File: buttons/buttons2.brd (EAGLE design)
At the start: 70 x 40 mm, 14 parts, among them U1 TINY2313

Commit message: I think I have a workable Cherry MX design
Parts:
- removed U1: TINY2313, avr-6:DIL20
- added U$1: TINY2313-*P*, avr-6:DIL20
- moved S6 166.9 mm to (55.0, 35.5)
- moved S5 143.9 mm to (39.0, 35.5)
- moved S3 124.5 mm to (55.0, 19.5)
- moved S4 121.0 mm to (23.0, 35.5)
- moved S2 102.7 mm to (39.0, 19.5)
- moved JP1 94.4 mm to (49.0, 7.91)
- moved S1 81.4 mm to (23.0, 19.5)
- moved C1 62.5 mm to (3.23, 8.81)
- moved SV1 23.0 mm to (26.1, 5.98), turned to 0 degrees
- moved STANDOFF3 4.44 mm to (66.2, 41.1)
- moved STANDOFF4 4.00 mm to (2.89, 41.1)
- moved STANDOFF1 1.12 mm to (66.2, 2.84)
- moved STANDOFF2 0.51 mm to (2.93, 2.84)
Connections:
- net BUTTON1: now also U$1.2; no longer U1.2
- net BUTTON2: now also U$1.3; no longer U1.3
- net BUTTON3: now also U$1.4; no longer U1.4
- net BUTTON4: now also U$1.5; no longer U1.5
- net BUTTON5: now also U$1.6; no longer U1.6
- net BUTTON6: now also U$1.7; no longer U1.7
- net GND: now also U$1.10; no longer U1.10
- net N$1: now also U$1.16; no longer U1.16
- net N$2: now also U$1.15; no longer U1.15
- net N$3: now also U$1.14; no longer U1.14
- net N$4: now also U$1.13; no longer U1.13
- net N$5: now also U$1.12; no longer U1.12
- net N$6: now also U$1.11; no longer U1.11
- net VCC: now also U$1.20; no longer U1.20
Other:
- board size 70 x 40 mm -> 69 x 44 mm

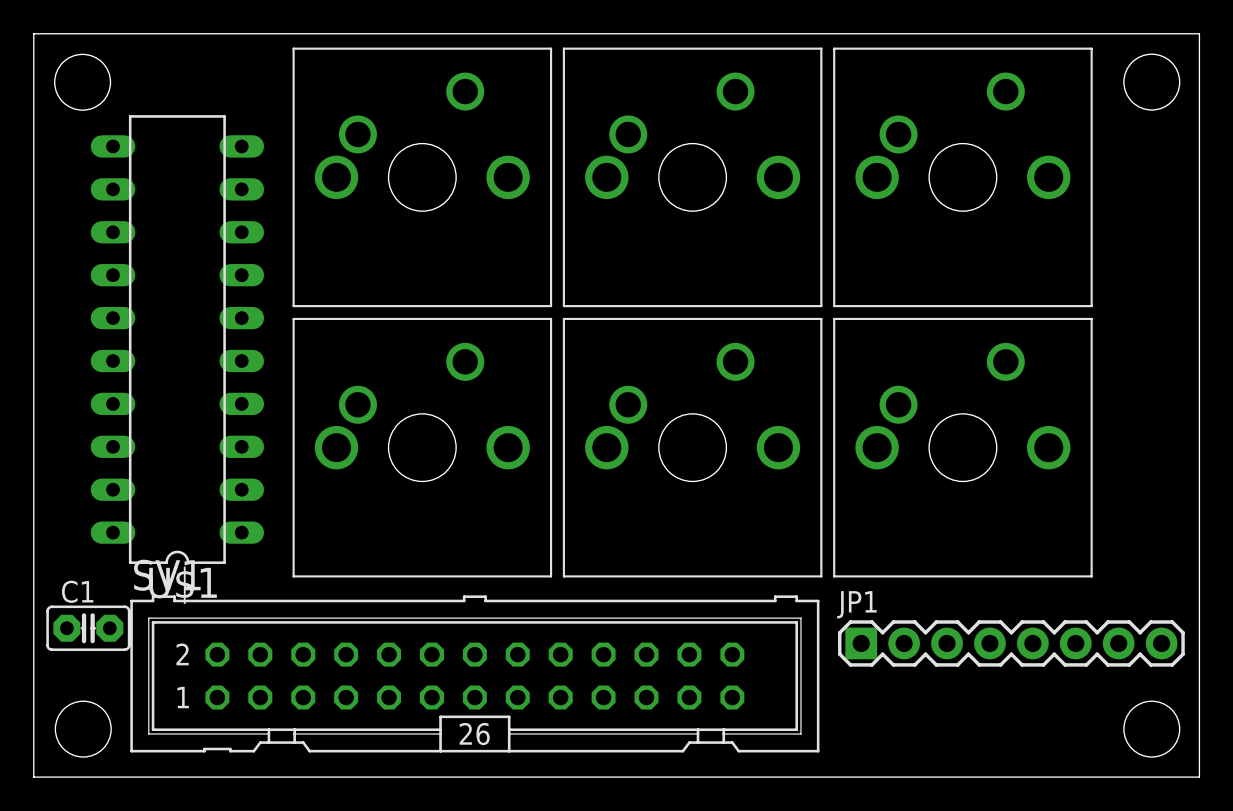
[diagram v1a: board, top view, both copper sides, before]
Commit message: working on signal routing
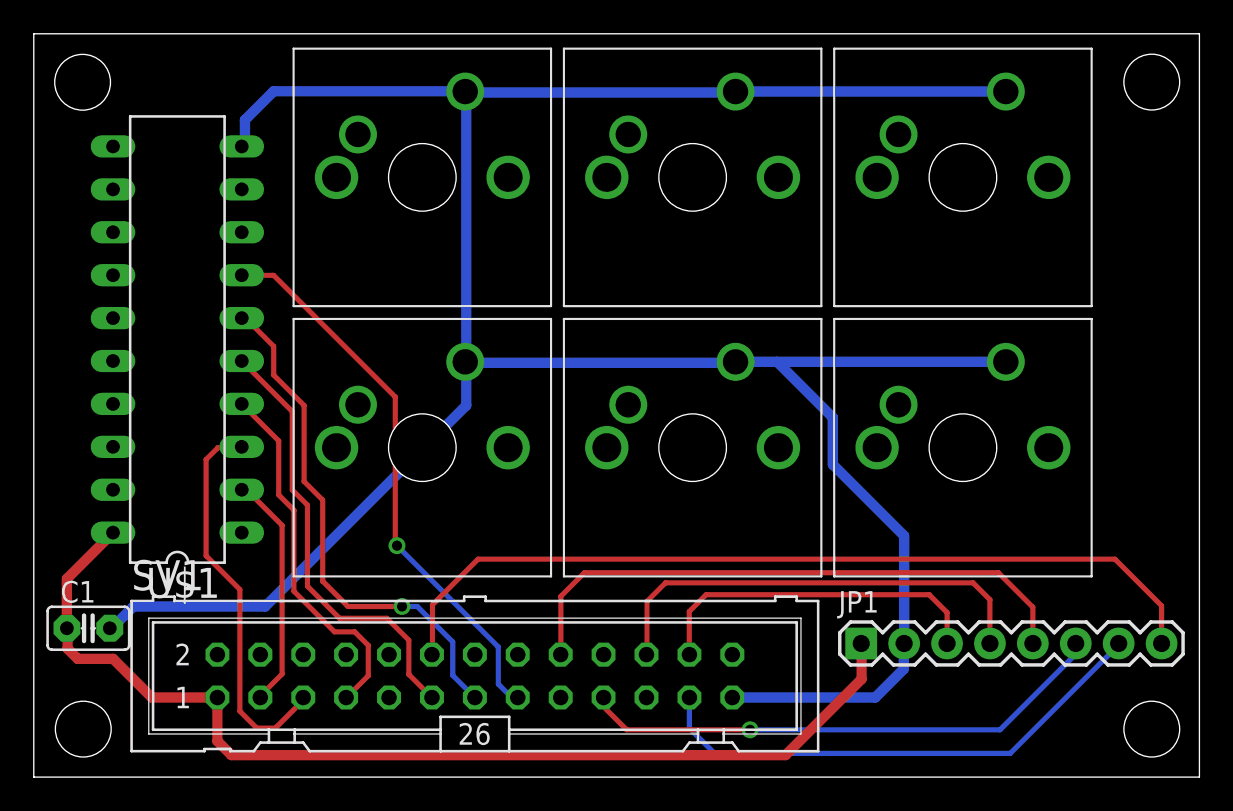
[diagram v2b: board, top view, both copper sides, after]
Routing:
- net GND: track 0.00 -> 156.8 mm
- net VCC: track 0.00 -> 63.1 mm
- net LED: track 0.00 -> 50.6 mm
- net DC: track 0.00 -> 35.0 mm
- net BUTTON6: track 0.00 -> 33.1 mm, vias 0 -> 1
- net MOSI: track 0.00 -> 31.6 mm, vias 0 -> 1
- net BUTTON5: track 0.00 -> 30.7 mm, vias 0 -> 1
- net SCK: track 0.00 -> 30.6 mm
- net RESET: track 0.00 -> 26.9 mm
- net BUTTON4: track 0.00 -> 26.2 mm
- net BUTTON2: track 0.00 -> 23.3 mm
- net BUTTON3: track 0.00 -> 21.7 mm
- net CS: track 0.00 -> 20.5 mm
- net BUTTON1: track 0.00 -> 14.0 mm

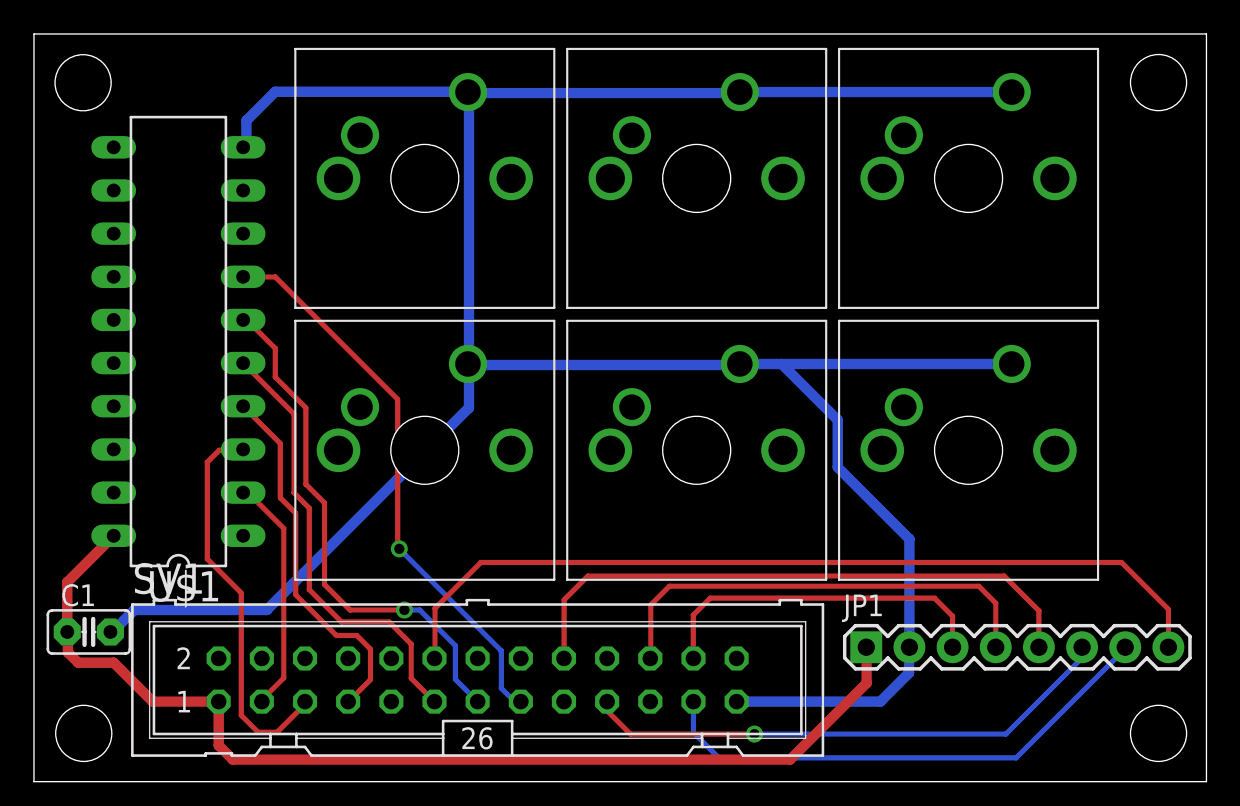
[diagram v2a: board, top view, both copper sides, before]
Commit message: rip up traces to buttons, move attiny2313
Buttons need to be mirrored because they will be
on the bottom of the board.

The attiny2313 was too close to the top left standoff.
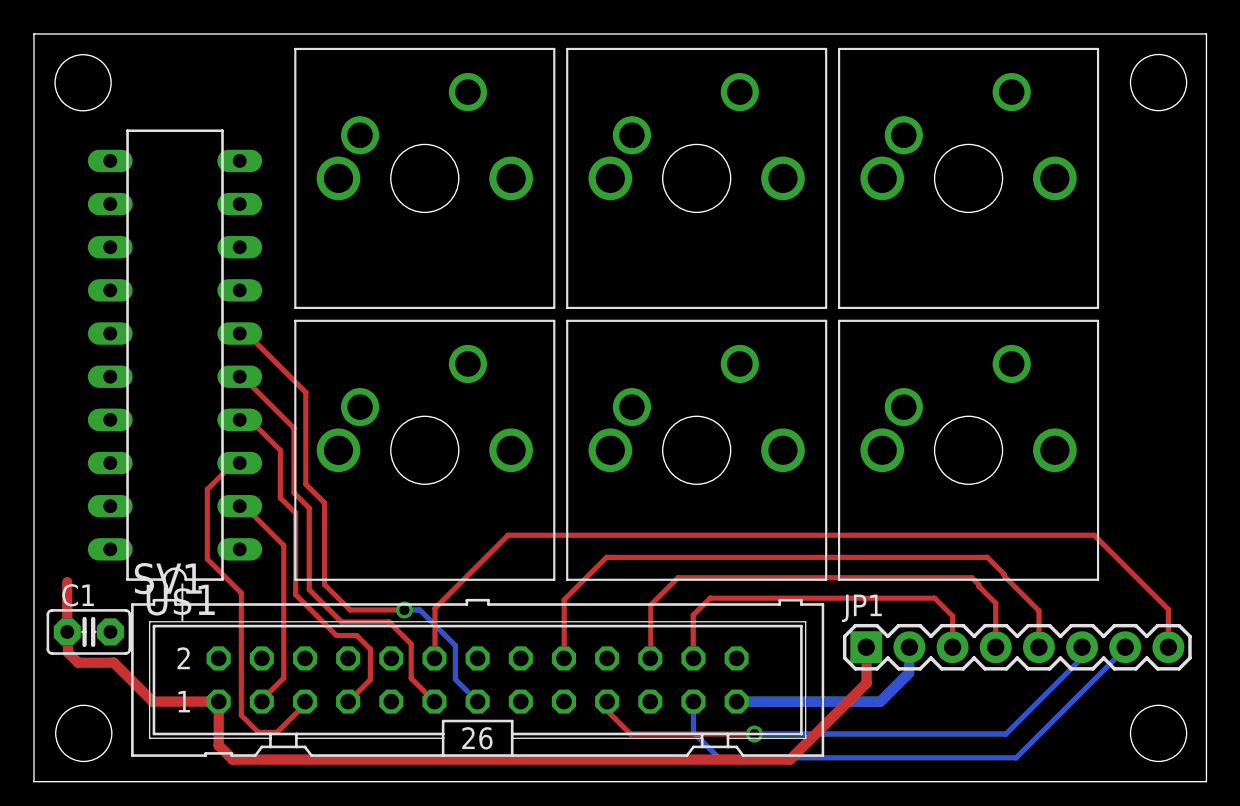
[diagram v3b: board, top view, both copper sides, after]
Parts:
- moved U$1 0.82 mm to (8.30, 25.1)
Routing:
- net GND: track 156.8 -> 12.4 mm
- net BUTTON6: track 33.1 -> 0.00 mm, vias 1 -> 0
- net VCC: track 63.1 -> 59.3 mm
- net BUTTON2: track 23.3 -> 21.8 mm
- net LED: track 50.6 -> 51.9 mm
- net DC: track 35.0 -> 35.9 mm
- net BUTTON4: track 26.2 -> 25.5 mm
- net BUTTON1: track 14.0 -> 13.3 mm
- net BUTTON5: track 30.7 -> 30.1 mm

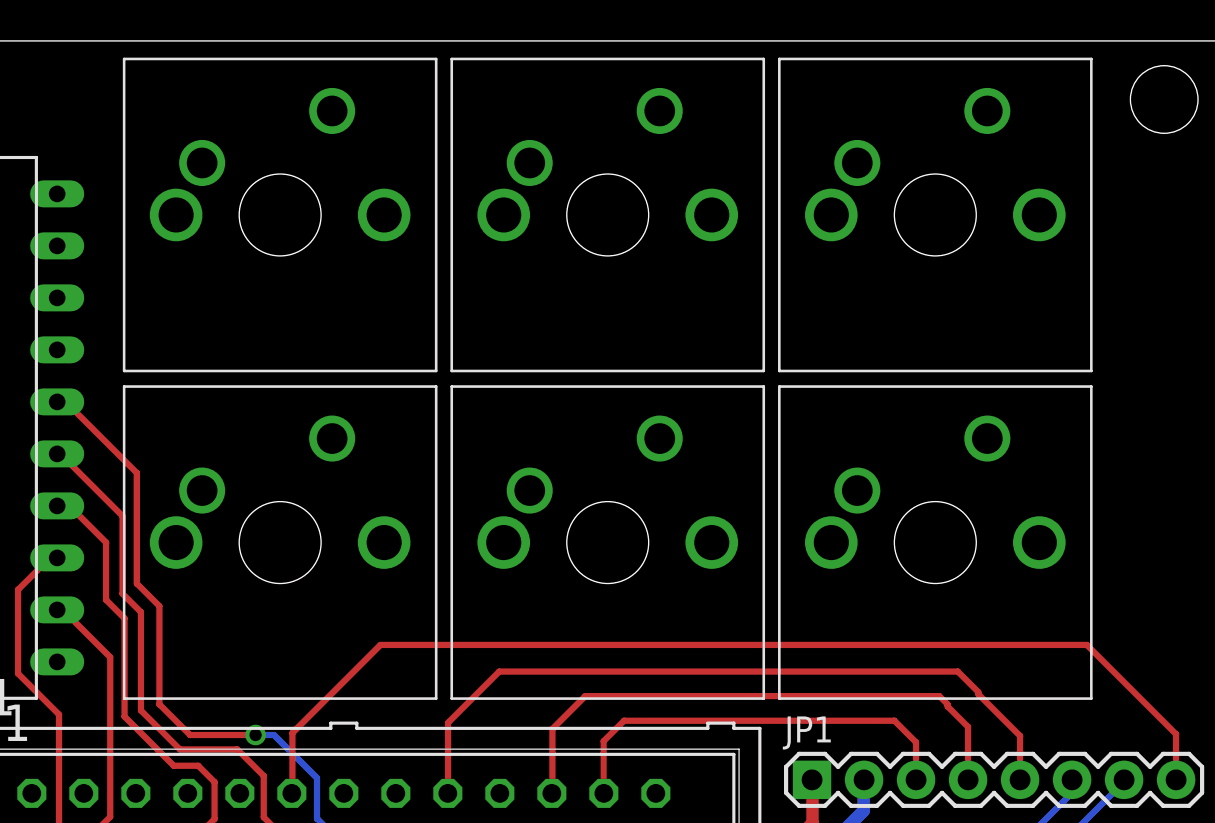
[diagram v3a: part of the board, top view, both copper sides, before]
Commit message: mirrored buttons
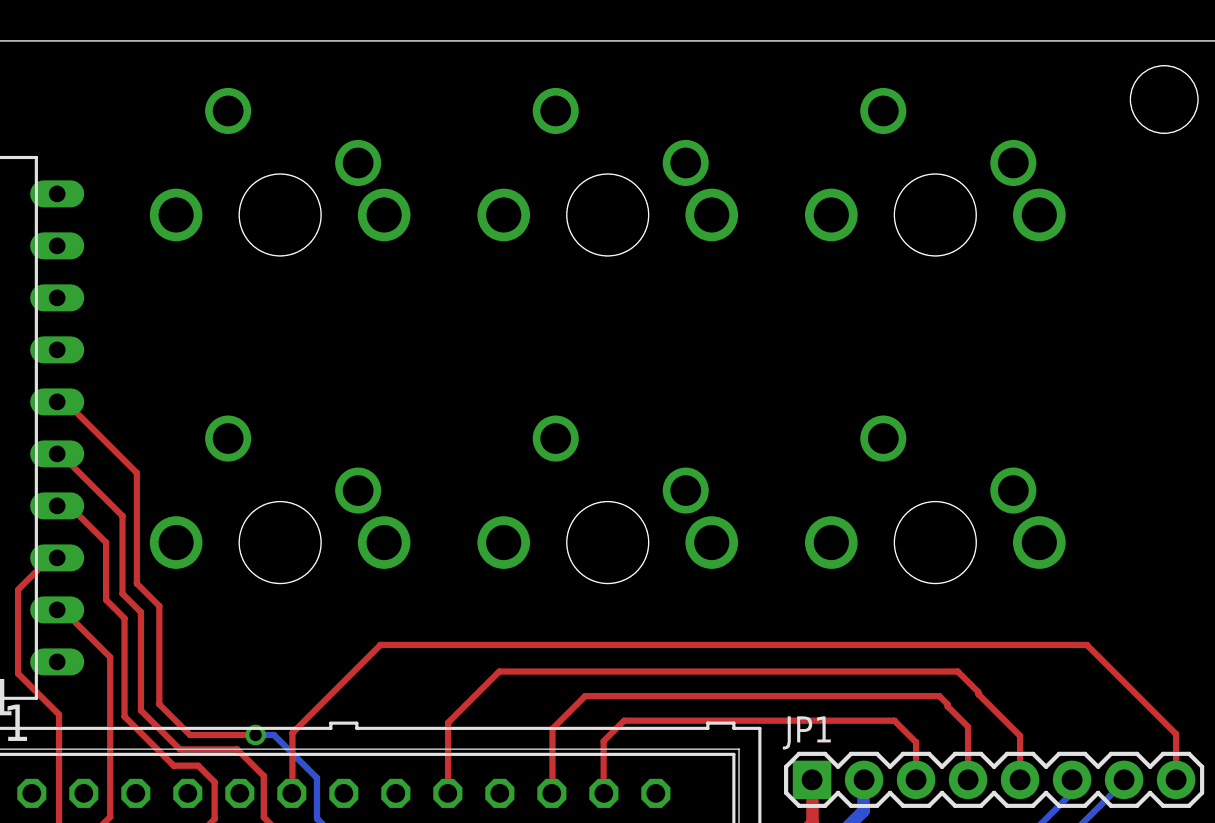
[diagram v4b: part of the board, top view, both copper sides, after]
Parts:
- flipped S1 to the bottom
- flipped S2 to the bottom
- flipped S3 to the bottom
- flipped S4 to the bottom
- flipped S5 to the bottom
- flipped S6 to the bottom
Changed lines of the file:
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@@
 <element name="STANDOFF3" library="SparkFun-Electromechanical" package="STAND-OFF" value="STAND-OFF" x="66.18" y="41.14"/>
 <element name="STANDOFF4" library="SparkFun-Electromechanical" package="STAND-OFF" value="STAND-OFF" x="2.89" y="41.13"/>
-<element name="S1" library="cherrymx" package="CHERRY-MX-I" value="CHERRY-MX-I" x="23" y="19.5"/>
-<element name="S2" library="cherrymx" package="CHERRY-MX-I" value="CHERRY-MX-I" x="39" y="19.5"/>
-<element name="S3" library="cherrymx" package="CHERRY-MX-I" value="CHERRY-MX-I" x="55" y="19.5"/>
-<element name="S4" library="cherrymx" package="CHERRY-MX-I" value="CHERRY-MX-I" x="23" y="35.5"/>
-<element name="S5" library="cherrymx" package="CHERRY-MX-I" value="CHERRY-MX-I" x="39" y="35.5"/>
-<element name="S6" library="cherrymx" package="CHERRY-MX-I" value="CHERRY-MX-I" x="55" y="35.5"/>
+<element name="S1" library="cherrymx" package="CHERRY-MX-I" value="CHERRY-MX-I" x="23" y="19.5" rot="MR0"/>
+<element name="S2" library="cherrymx" package="CHERRY-MX-I" value="CHERRY-MX-I" x="39" y="19.5" rot="MR0"/>
+<element name="S3" library="cherrymx" package="CHERRY-MX-I" value="CHERRY-MX-I" x="55" y="19.5" rot="MR0"/>
+<element name="S4" library="cherrymx" package="CHERRY-MX-I" value="CHERRY-MX-I" x="23" y="35.5" rot="MR0"/>
+<element name="S5" library="cherrymx" package="CHERRY-MX-I" value="CHERRY-MX-I" x="39" y="35.5" rot="MR0"/>
+<element name="S6" library="cherrymx" package="CHERRY-MX-I" value="CHERRY-MX-I" x="55" y="35.5" rot="MR0"/>
 <element name="U$1" library="avr-6" package="DIL20" value="TINY2313-*P*" x="8.3" y="25.1" rot="R90"/>
 </elements>
@@
 <wire x1="51.5" y1="6.4" x2="51.5" y2="7.89" width="0.6096" layer="16"/>
 <wire x1="51.5" y1="7.89" x2="51.52" y2="7.91" width="0.6096" layer="16"/>
-<wire x1="41.54" y1="40.58" x2="57.54" y2="40.58" width="0" layer="19" extent="1-1"/>
-<wire x1="57.54" y1="24.58" x2="57.54" y2="40.58" width="0" layer="19" extent="1-1"/>
-<wire x1="25.54" y1="40.58" x2="41.54" y2="40.58" width="0" layer="19" extent="1-1"/>
-<wire x1="12.11" y1="36.53" x2="25.54" y2="40.58" width="0" layer="19" extent="1-1"/>
-<wire x1="41.54" y1="24.58" x2="41.54" y2="40.58" width="0" layer="19" extent="1-1"/>
-<wire x1="25.54" y1="24.58" x2="25.54" y2="40.58" width="0" layer="19" extent="1-1"/>
-<wire x1="51.52" y1="7.91" x2="57.54" y2="24.58" width="0" layer="19" extent="1-1"/>
-<wire x1="4.5" y1="8.81" x2="25.54" y2="24.58" width="0" layer="19" extent="1-1"/>
+<wire x1="36.46" y1="40.58" x2="52.46" y2="40.58" width="0" layer="19" extent="1-1"/>
+<wire x1="52.46" y1="24.58" x2="52.46" y2="40.58" width="0" layer="19" extent="1-1"/>
+<wire x1="20.46" y1="40.58" x2="36.46" y2="40.58" width="0" layer="19" extent="1-1"/>
+<wire x1="12.11" y1="36.53" x2="20.46" y2="40.58" width="0" layer="19" extent="1-1"/>
+<wire x1="36.46" y1="24.58" x2="36.46" y2="40.58" width="0" layer="19" extent="1-1"/>
+<wire x1="20.46" y1="24.58" x2="20.46" y2="40.58" width="0" layer="19" extent="1-1"/>
+<wire x1="51.52" y1="7.91" x2="52.46" y2="24.58" width="0" layer="19" extent="1-1"/>
+<wire x1="4.5" y1="8.81" x2="20.46" y2="24.58" width="0" layer="19" extent="1-1"/>
 </signal>
 <signal name="N$1">
 <contactref element="S6" pad="PIN-1"/>
 <contactref element="U$1" pad="16"/>
-<wire x1="4.49" y1="23.83" x2="51.19" y2="38.04" width="0" layer="19" extent="1-1"/>
+<wire x1="4.49" y1="23.83" x2="58.81" y2="38.04" width="0" layer="19" extent="1-1"/>
 </signal>
 <signal name="N$2">
 <contactref element="S5" pad="PIN-1"/>
 <contactref element="U$1" pad="15"/>
-<wire x1="4.49" y1="26.37" x2="35.19" y2="38.04" width="0" layer="19" extent="1-1"/>
+<wire x1="4.49" y1="26.37" x2="42.81" y2="38.04" width="0" layer="19" extent="1-1"/>
 </signal>
 <signal name="N$3">
 <contactref element="S4" pad="PIN-1"/>
 <contactref element="U$1" pad="14"/>
-<wire x1="4.49" y1="28.91" x2="19.19" y2="38.04" width="0" layer="19" extent="1-1"/>
+<wire x1="4.49" y1="28.91" x2="26.81" y2="38.04" width="0" layer="19" extent="1-1"/>
 </signal>
 <signal name="N$4">
 <contactref element="S3" pad="PIN-1"/>
 <contactref element="U$1" pad="13"/>
-<wire x1="4.49" y1="31.45" x2="51.19" y2="22.04" width="0" layer="19" extent="1-1"/>
+<wire x1="4.49" y1="31.45" x2="58.81" y2="22.04" width="0" layer="19" extent="1-1"/>
 </signal>
 <signal name="N$5">
 <contactref element="S2" pad="PIN-1"/>
 <contactref element="U$1" pad="12"/>
-<wire x1="4.49" y1="33.99" x2="35.19" y2="22.04" width="0" layer="19" extent="1-1"/>
+<wire x1="4.49" y1="33.99" x2="42.81" y2="22.04" width="0" layer="19" extent="1-1"/>
 </signal>
 <signal name="N$6">
 <contactref element="S1" pad="PIN-1"/>
 <contactref element="U$1" pad="11"/>
-<wire x1="4.49" y1="36.53" x2="19.19" y2="22.04" width="0" layer="19" extent="1-1"/>
+<wire x1="4.49" y1="36.53" x2="26.81" y2="22.04" width="0" layer="19" extent="1-1"/>
 </signal>
 <signal name="VCC">
